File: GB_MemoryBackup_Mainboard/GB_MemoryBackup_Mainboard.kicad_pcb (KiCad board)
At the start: 2 copper layers, 55.5 x 135.5 mm, 25 parts, among them J1 GB_Cart_EdgeConn-1Row-32Pins, J3 JTAG-A, J4 Conn_02x16_Odd_Even, SW1 SW_SPDT, U1 AT29C010A-PLCC32, U2 28SF040-120-4C-NH-PLCC32, U3 Generic-ATF15xx-PLCC44, U4 TC551001BPL_DIP32, U5 BA6162F, U6 74HC373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

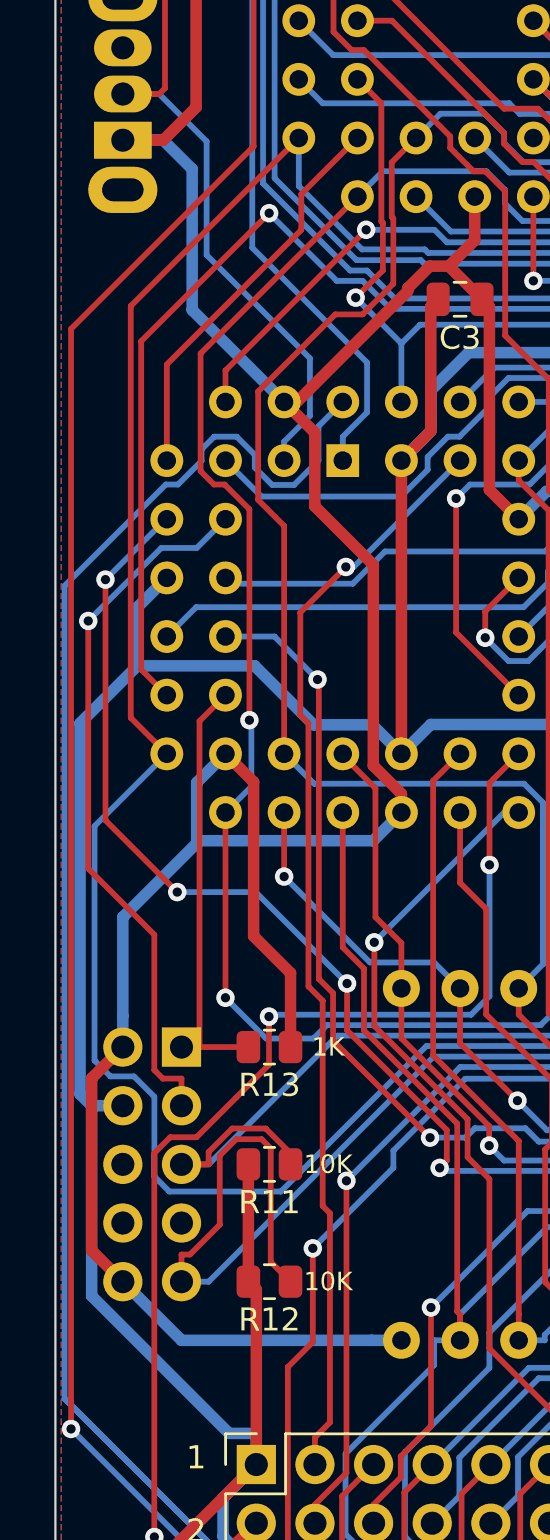
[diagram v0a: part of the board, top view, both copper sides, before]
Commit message: Modified: Swapped SW_1 and SW_2/ARST on PCB project.
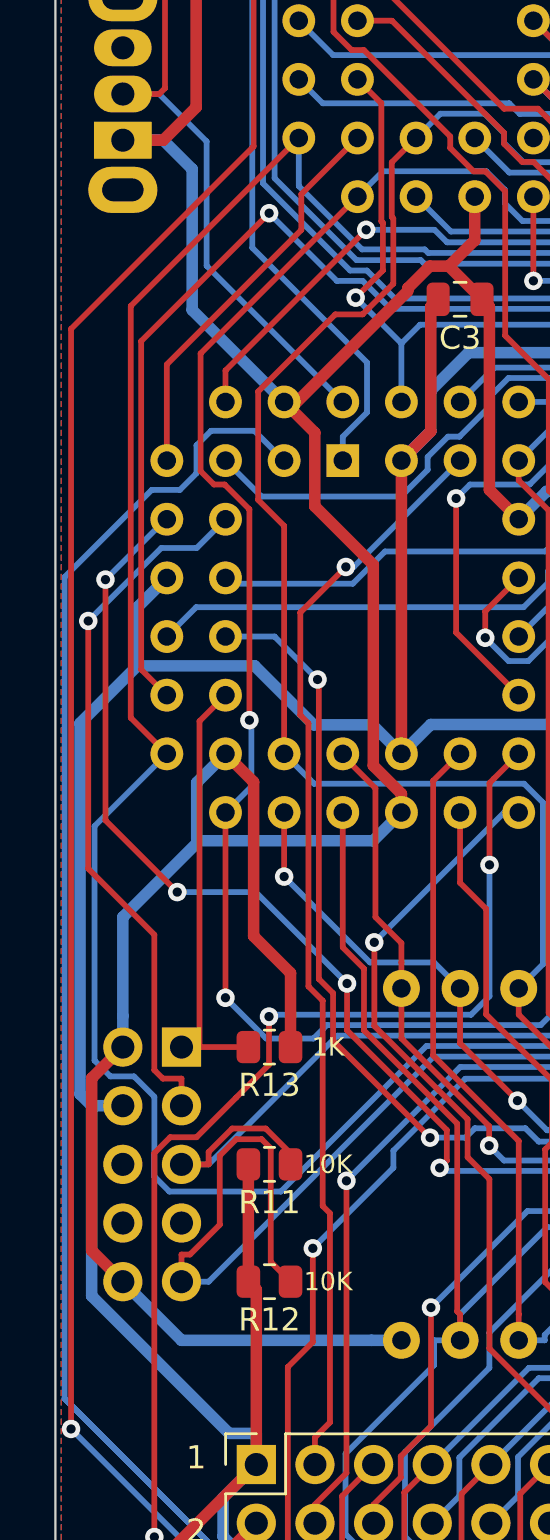
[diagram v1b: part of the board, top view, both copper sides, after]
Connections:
- U3 pad 43: /~SW_1 -> /~ARST
- U3 pad 44: /~ARST -> /~SW_1
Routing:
- net /~ARST: track 187.8 -> 182.9 mm
- net /~SW_1: track 31.2 -> 28.8 mm

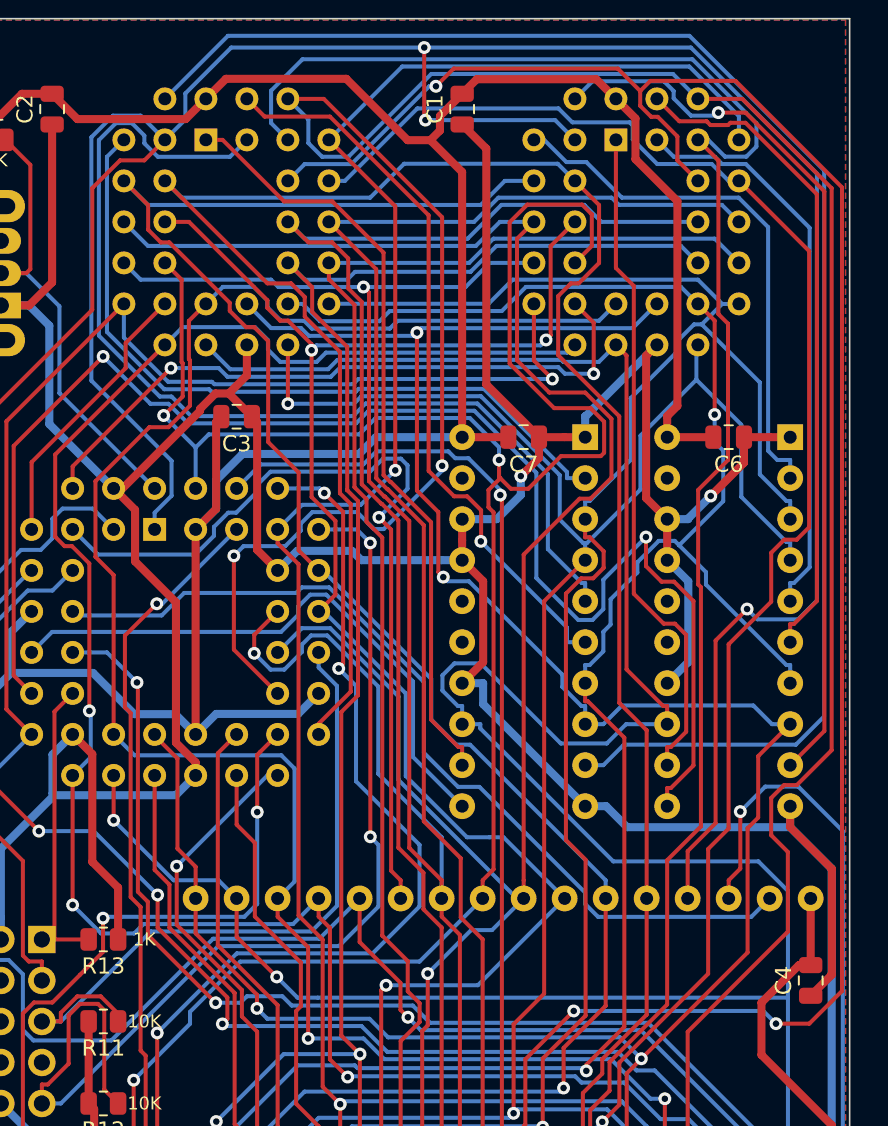
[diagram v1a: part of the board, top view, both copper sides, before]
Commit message: Modified: Manually revised routing of several tracks.
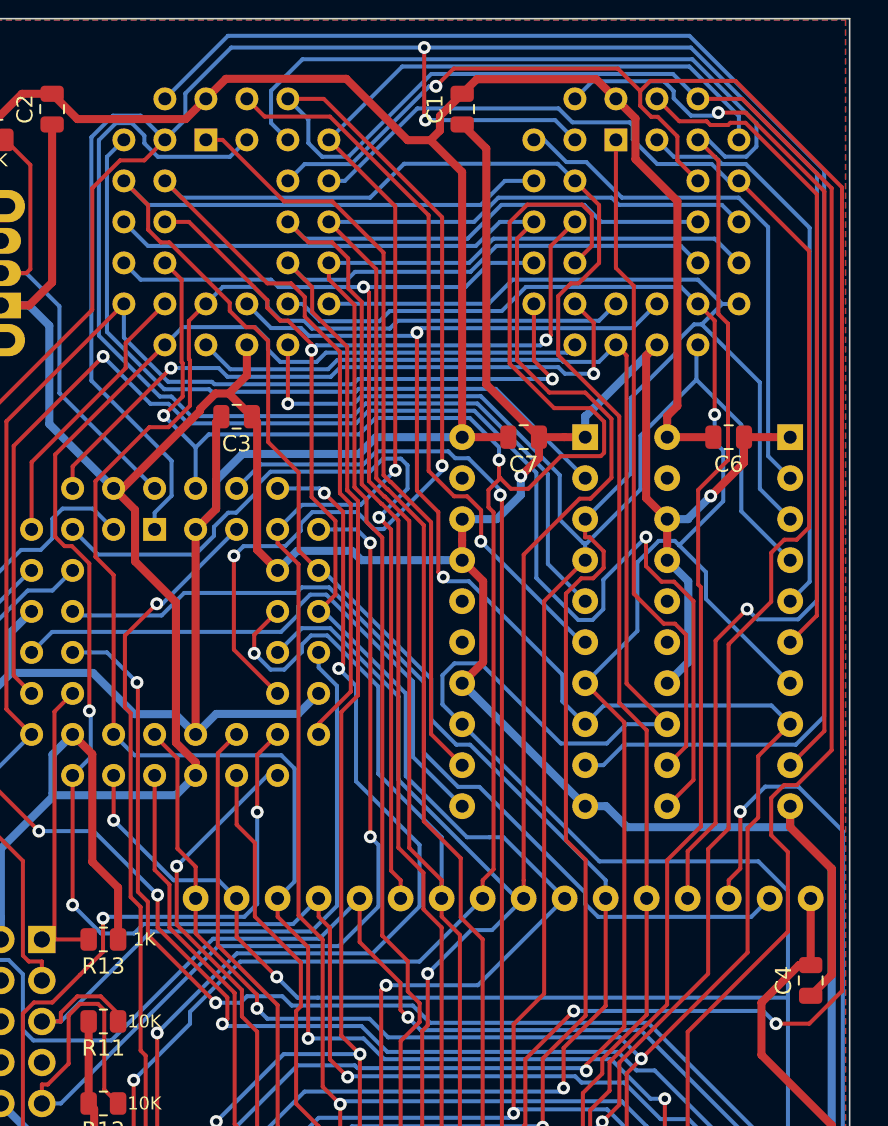
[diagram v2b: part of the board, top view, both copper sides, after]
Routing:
- net GND: track 425.4 -> 424.6 mm
- net /F040_A16: track 45.9 -> 45.3 mm

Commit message: Modified: PCB for v1.4 schematic.(Unrouted yet.)
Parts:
- removed C6: 0.1uF, Capacitor_SMD:C_0805_2012Metric
- removed the G*** at (88.3, 123.2)
- removed U6: 74HC373, Package_DIP:DIP-20_W7.62mm_Socket
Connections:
- U3 pad 11: /AA9 -> /AA15
- U3 pad 12: /AA10 -> /AD0
- U3 pad 14: /AA11 -> /AD1
- U3 pad 16: /AA12 -> /AD2
- U3 pad 17: /AA13 -> /AD3
- U3 pad 18: /AA14 -> /AD4
- U3 pad 19: /AA15 -> /AD5
- U3 pad 20: /AD0 -> /AD6
- U3 pad 21: /AD1 -> /AD7
- U3 pad 24: /AD2 -> /~RAM_CE
- U3 pad 25: /AD3 -> /RAM_A14
- U3 pad 26: /AD4 -> /RAM_A15
- U3 pad 27: /AD5 -> /RAM_A16
- U3 pad 28: /AD6 -> /HC373_040_LE
- U3 pad 29: /AD7 -> (no net)
- U3 pad 31: /HC373_010_LE -> /~F_CE_010
- U3 pad 33: /HC373_040_LE -> /F010_A14
- U3 pad 34: /RAM_A16 -> /F010_A15
- U3 pad 36: /RAM_A15 -> /F010_A16
- U3 pad 37: /RAM_A14 -> /F010_A17
- U3 pad 39: /~F_CE_040 -> /F010_A18
- U3 pad 4: /AA15_T -> /~AWR_T
- U3 pad 40: /~F_CE_010 -> /~F_CE_040
- U3 pad 41: /~RAM_CE -> /AA15_T
- U3 pad 5: /~AWR_T -> /~ARD_T
- U3 pad 6: /~ARD_T -> /AA0
- U3 pad 8: /AA7 -> /AA13
- U3 pad 9: /AA8 -> /AA14
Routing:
- net GND: track 424.6 -> 0.00 mm, vias 4 -> 0
- net +5V: track 336.5 -> 0.00 mm, vias 1 -> 0
- net /~AWR: track 288.3 -> 0.00 mm, vias 5 -> 0
- net /AD4: track 248.6 -> 0.00 mm, vias 2 -> 0
- net /AA12: track 246.5 -> 0.00 mm, vias 2 -> 0
- net /AD2: track 244.7 -> 0.00 mm, vias 2 -> 0
- net /AD7: track 224.3 -> 0.00 mm, vias 2 -> 0
- net /AD1: track 221.0 -> 0.00 mm, vias 2 -> 0
- net /AD3: track 220.5 -> 0.00 mm, vias 4 -> 0
- net /AD0: track 214.5 -> 0.00 mm, vias 1 -> 0
- net /AA13: track 212.6 -> 0.00 mm, vias 1 -> 0
- net /AA4: track 210.8 -> 0.00 mm, vias 3 -> 0
- net /~ARD: track 203.7 -> 0.00 mm, vias 3 -> 0
- net /AA8: track 203.2 -> 0.00 mm, vias 1 -> 0
- net /AD6: track 197.9 -> 0.00 mm, vias 3 -> 0
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- removed copper zone on F.Cu, net +5V
- removed copper zone on B.Cu, net GND

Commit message: Modified: v1.4 PCB routed and manually revised.
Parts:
- added G***: LOGO, LogoGraphics:MaskLayer_12mm_x_12mm_ShadowSonic, B.Cu at (88.3, 123.2)
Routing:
- net GND: track 0.00 -> 369.1 mm, vias 0 -> 2
- net +5V: track 0.00 -> 310.7 mm, vias 0 -> 3
- net /~AWR: track 0.00 -> 279.2 mm, vias 0 -> 3
- net /AA8: track 0.00 -> 226.6 mm, vias 0 -> 4
- net /AD3: track 0.00 -> 224.4 mm, vias 0 -> 3
- net /AD2: track 0.00 -> 220.4 mm, vias 0 -> 1
- net /AA13: track 0.00 -> 206.4 mm, vias 0 -> 3
- net /AA2: track 0.00 -> 204.7 mm, vias 0 -> 2
- net /AD4: track 0.00 -> 199.1 mm, vias 0 -> 2
- net /AD7: track 0.00 -> 189.3 mm, vias 0 -> 2
- net /AD1: track 0.00 -> 186.6 mm, vias 0 -> 2
- net /AD6: track 0.00 -> 186.4 mm, vias 0 -> 4
- net /AA6: track 0.00 -> 186.0 mm
- net /AD5: track 0.00 -> 185.1 mm, vias 0 -> 5
- net /AA4: track 0.00 -> 184.2 mm, vias 0 -> 1
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- added copper zone on F.Cu, net +5V
- added copper zone on B.Cu, net GND
